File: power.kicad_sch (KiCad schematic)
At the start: 4 parts, among them U701 LP2951-3.3_SOIC

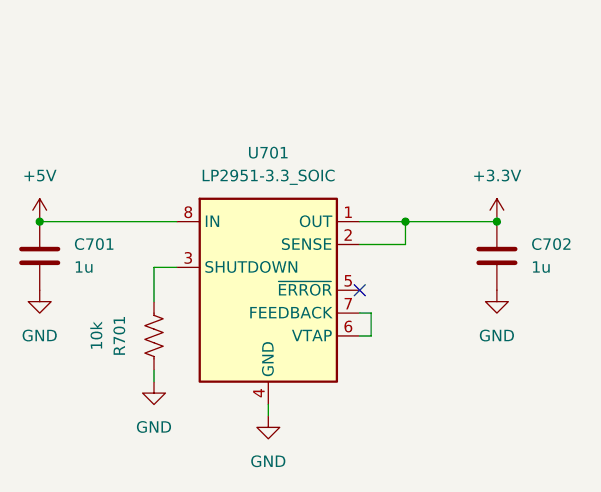
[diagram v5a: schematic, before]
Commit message: Add partnumbers
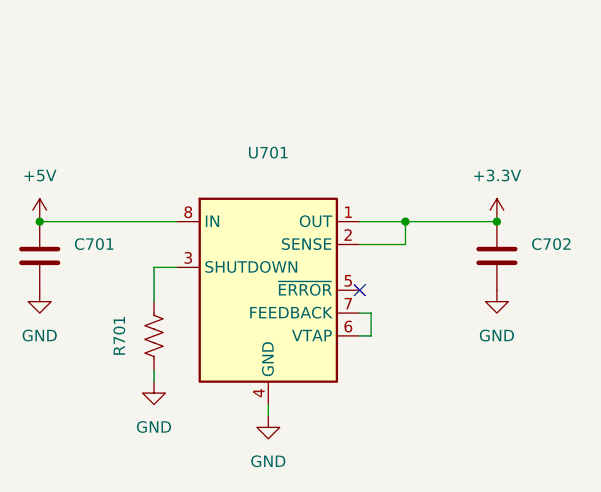
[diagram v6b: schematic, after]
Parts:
- C701, C702: value 1u -> (none); footprint Capacitor_SMD:C_0805_2012Metric -> (none); Manufacturer (none) -> Generic; PartNumber (none) -> Generic
- R701: value 10k -> (none); footprint Resistor_SMD:R_0805_2012Metric -> (none); Manufacturer (none) -> Generic; PartNumber (none) -> Generic
- U701: value LP2951-3.3_SOIC -> (none); footprint Package_SO:SOIC-8_3.9x4.9mm_P1.27mm -> (none); Manufacturer (none) -> Texas Instrument; PartNumber (none) -> LP2951-33D
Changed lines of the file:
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@@
       (effects (font (size 1.27 1.27)) (justify left))
     )
-    (property "Value" "1u" (id 1) (at 184.15 68.5799 0)
+    (property "Value" "" (id 1) (at 184.15 68.5799 0)
       (effects (font (size 1.27 1.27)) (justify left))
     )
-    (property "Footprint" "Capacitor_SMD:C_0805_2012Metric" (id 2) (at 181.3052 71.12 0)
+    (property "Footprint" "" (id 2) (at 181.3052 71.12 0)
       (effects (font (size 1.27 1.27)) hide)
     )
     (property "Datasheet" "~" (id 3) (at 180.34 67.31 0)
+      (effects (font (size 1.27 1.27)) hide)
+    )
+    (property "Manufacturer" "Generic" (id 4) (at 180.34 67.31 0)
+      (effects (font (size 1.27 1.27)) hide)
+    )
+    (property "PartNumber" "Generic" (id 5) (at 180.34 67.31 0)
       (effects (font (size 1.27 1.27)) hide)
     )
@@
       (effects (font (size 1.27 1.27)) (justify left))
     )
-    (property "Value" "1u" (id 1) (at 133.35 68.5799 0)
+    (property "Value" "" (id 1) (at 133.35 68.5799 0)
       (effects (font (size 1.27 1.27)) (justify left))
     )
-    (property "Footprint" "Capacitor_SMD:C_0805_2012Metric" (id 2) (at 130.5052 71.12 0)
+    (property "Footprint" "" (id 2) (at 130.5052 71.12 0)
       (effects (font (size 1.27 1.27)) hide)
     )
     (property "Datasheet" "~" (id 3) (at 129.54 67.31 0)
+      (effects (font (size 1.27 1.27)) hide)
+    )
+    (property "Manufacturer" "Generic" (id 4) (at 129.54 67.31 0)
+      (effects (font (size 1.27 1.27)) hide)
+    )
+    (property "PartNumber" "Generic" (id 5) (at 129.54 67.31 0)
       (effects (font (size 1.27 1.27)) hide)
     )
@@
     (in_bom yes) (on_board yes) (fields_autoplaced)
     (property "Reference" "U701" (id 0) (at 154.94 55.88 0))
-    (property "Value" "LP2951-3.3_SOIC" (id 1) (at 154.94 58.42 0))
-    (property "Footprint" "Package_SO:SOIC-8_3.9x4.9mm_P1.27mm" (id 2) (at 154.94 87.63 0)
+    (property "Value" "" (id 1) (at 154.94 58.42 0))
+    (property "Footprint" "" (id 2) (at 154.94 87.63 0)
       (effects (font (size 1.27 1.27)) hide)
     )
     (property "Datasheet" "http://www.ti.com/lit/ds/symlink/lp2951.pdf" (id 3) (at 154.94 71.12 0)
+      (effects (font (size 1.27 1.27)) hide)
+    )
+    (property "Manufacturer" "Texas Instrument" (id 4) (at 154.94 71.12 0)
+      (effects (font (size 1.27 1.27)) hide)
+    )
+    (property "PartNumber" "LP2951-33D" (id 5) (at 154.94 71.12 0)
       (effects (font (size 1.27 1.27)) hide)
     )
@@
     (in_bom yes) (on_board yes)
     (property "Reference" "R701" (id 0) (at 138.43 76.2 90))
-    (property "Value" "10k" (id 1) (at 135.89 76.2 90))
-    (property "Footprint" "Resistor_SMD:R_0805_2012Metric" (id 2) (at 143.256 76.454 90)
+    (property "Value" "" (id 1) (at 135.89 76.2 90))
+    (property "Footprint" "" (id 2) (at 143.256 76.454 90)
       (effects (font (size 1.27 1.27)) hide)
     )
@@
       (effects (font (size 1.27 1.27)) hide)
     )
+    (property "Manufacturer" "Generic" (id 4) (at 142.24 76.2 0)
+      (effects (font (size 1.27 1.27)) hide)
+    )
+    (property "PartNumber" "Generic" (id 5) (at 142.24 76.2 0)
+      (effects (font (size 1.27 1.27)) hide)
+    )

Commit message: Fix missing footprints in schematic
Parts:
- C701, C702, R701: now left out of the parts list
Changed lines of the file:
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@@
   )
   (symbol (lib_id "Device:C") (at 180.34 67.31 0) (unit 1)
-    (in_bom yes) (on_board yes) (fields_autoplaced)
+    (in_bom no) (on_board yes) (fields_autoplaced)
     (property "Reference" "C702" (id 0) (at 184.15 66.0399 0)
       (effects (font (size 1.27 1.27)) (justify left))
@@
   )
   (symbol (lib_id "Device:C") (at 129.54 67.31 0) (unit 1)
-    (in_bom yes) (on_board yes) (fields_autoplaced)
+    (in_bom no) (on_board yes) (fields_autoplaced)
     (property "Reference" "C701" (id 0) (at 133.35 66.0399 0)
       (effects (font (size 1.27 1.27)) (justify left))
@@
   )
   (symbol (lib_id "Device:R_US") (at 142.24 76.2 0) (unit 1)
-    (in_bom yes) (on_board yes)
+    (in_bom no) (on_board yes)
     (property "Reference" "R701" (id 0) (at 138.43 76.2 90))
     (property "Value" "" (id 1) (at 135.89 76.2 90))

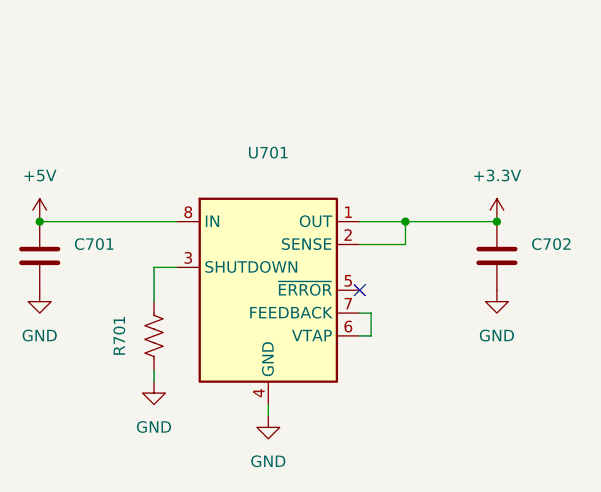
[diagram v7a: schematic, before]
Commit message: Add feedback resistors for regulator
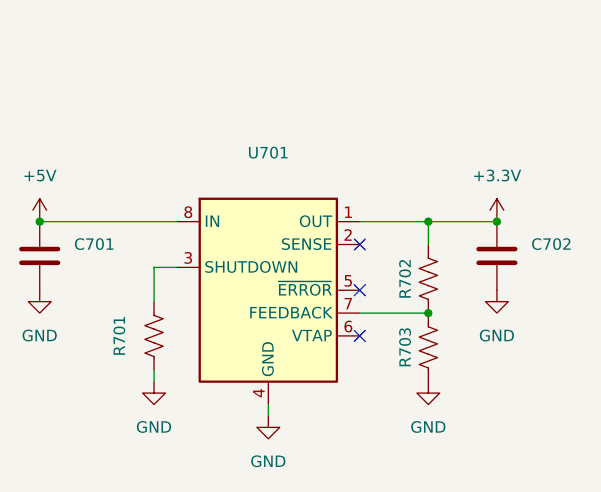
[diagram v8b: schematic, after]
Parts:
- added R702, R703: (no value), symbol Device:R_US
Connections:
- net +3V3: now also R702.1; no longer U701.2 (SENSE)
- net GND: now also R703.2
- net at U701.7 (FEEDBACK): now also R702.2, R703.1; no longer U701.6 (VTAP)
- no-connect marks 1 -> 3
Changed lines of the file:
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@@
   (junction (at 129.54 63.5) (diameter 0) (color 0 0 0 0)
   )
-  (junction (at 170.18 63.5) (diameter 0) (color 0 0 0 0)
+  (junction (at 172.72 73.66) (diameter 0) (color 0 0 0 0)
   )
   (junction (at 180.34 63.5) (diameter 0) (color 0 0 0 0)
   )
+  (junction (at 172.72 63.5) (diameter 0) (color 0 0 0 0)
+  )
+  (no_connect (at 165.1 66.04))
   (no_connect (at 165.1 71.12))
+  (no_connect (at 165.1 76.2))
   (wire (pts (xy 142.24 68.58) (xy 144.78 68.58))
     (stroke (width 0) (type default) (color 0 0 0 0))
   )
-  (wire (pts (xy 165.1 63.5) (xy 170.18 63.5))
-    (stroke (width 0) (type default) (color 0 0 0 0))
-  )
-  (wire (pts (xy 170.18 63.5) (xy 170.18 66.04))
-    (stroke (width 0) (type default) (color 0 0 0 0))
-  )
-  (wire (pts (xy 166.37 73.66) (xy 165.1 73.66))
+  (wire (pts (xy 165.1 73.66) (xy 172.72 73.66))
     (stroke (width 0) (type default) (color 0 0 0 0))
   )
   (wire (pts (xy 129.54 63.5) (xy 144.78 63.5))
-    (stroke (width 0) (type default) (color 0 0 0 0))
-  )
-  (wire (pts (xy 166.37 76.2) (xy 165.1 76.2))
-    (stroke (width 0) (type default) (color 0 0 0 0))
-  )
-  (wire (pts (xy 170.18 66.04) (xy 165.1 66.04))
     (stroke (width 0) (type default) (color 0 0 0 0))
   )
@@
     (stroke (width 0) (type default) (color 0 0 0 0))
   )
-  (wire (pts (xy 180.34 63.5) (xy 170.18 63.5))
+  (wire (pts (xy 165.1 63.5) (xy 172.72 63.5))
     (stroke (width 0) (type default) (color 0 0 0 0))
   )
-  (wire (pts (xy 166.37 73.66) (xy 166.37 76.2))
+  (wire (pts (xy 172.72 63.5) (xy 172.72 66.04))
+    (stroke (width 0) (type default) (color 0 0 0 0))
+  )
+  (wire (pts (xy 172.72 63.5) (xy 180.34 63.5))
     (stroke (width 0) (type default) (color 0 0 0 0))
   )
   (wire (pts (xy 142.24 80.01) (xy 142.24 81.28))
     (stroke (width 0) (type default) (color 0 0 0 0))
+  )
+  (symbol (lib_id "power:GND") (at 172.72 81.28 0) (unit 1)
+    (in_bom yes) (on_board yes) (fields_autoplaced)
+    (property "Reference" "#PWR?" (id 0) (at 172.72 87.63 0)
+      (effects (font (size 1.27 1.27)) hide)
+    )
+    (property "Value" "GND" (id 1) (at 172.72 86.36 0))
+    (property "Footprint" "" (id 2) (at 172.72 81.28 0)
+      (effects (font (size 1.27 1.27)) hide)
+    )
+    (property "Datasheet" "" (id 3) (at 172.72 81.28 0)
+      (effects (font (size 1.27 1.27)) hide)
+    )
+    (pin "1")
   )
   (symbol (lib_id "power:GND") (at 154.94 85.09 0) (unit 1)
@@
     (pin "2")
   )
+  (symbol (lib_id "Device:R_US") (at 172.72 69.85 0) (unit 1)
+    (in_bom no) (on_board yes)
+    (property "Reference" "R702" (id 0) (at 170.18 69.85 90))
+    (property "Value" "" (id 1) (at 175.26 69.85 90))
+    (property "Footprint" "" (id 2) (at 173.736 70.104 90)
+      (effects (font (size 1.27 1.27)) hide)
+    )
+    (property "Datasheet" "~" (id 3) (at 172.72 69.85 0)
+      (effects (font (size 1.27 1.27)) hide)
+    )
+    (property "Manufacturer" "Generic" (id 4) (at 172.72 69.85 0)
+      (effects (font (size 1.27 1.27)) hide)
+    )
+    (property "PartNumber" "Generic" (id 5) (at 172.72 69.85 0)
+      (effects (font (size 1.27 1.27)) hide)
+    )
+    (pin "1")
+    (pin "2")
+  )
   (symbol (lib_id "power:GND") (at 129.54 71.12 0) (unit 1)
     (in_bom yes) (on_board yes) (fields_autoplaced)
@@
     (pin "1")
   )
+  (symbol (lib_id "Device:R_US") (at 172.72 77.47 0) (unit 1)
+    (in_bom no) (on_board yes)
+    (property "Reference" "R703" (id 0) (at 170.18 77.47 90))
+    (property "Value" "" (id 1) (at 175.26 77.47 90))
+    (property "Footprint" "" (id 2) (at 173.736 77.724 90)
+      (effects (font (size 1.27 1.27)) hide)
+    )
+    (property "Datasheet" "~" (id 3) (at 172.72 77.47 0)
+      (effects (font (size 1.27 1.27)) hide)
+    )
+    (property "Manufacturer" "Generic" (id 4) (at 172.72 77.47 0)
+      (effects (font (size 1.27 1.27)) hide)
+    )
+    (property "PartNumber" "Generic" (id 5) (at 172.72 77.47 0)
+      (effects (font (size 1.27 1.27)) hide)
+    )
+    (pin "1")
+    (pin "2")
+  )
   (symbol (lib_id "power:+5V") (at 129.54 63.5 0) (unit 1)
